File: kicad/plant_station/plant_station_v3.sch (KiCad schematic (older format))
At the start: 12 parts, among them J10 I2C HOST, J13 MB_I2C, J2 MB_I2C, J4 MB_I2C, J5 MB_I2C, J6 MB_I2C, J9 I2C SCREEN

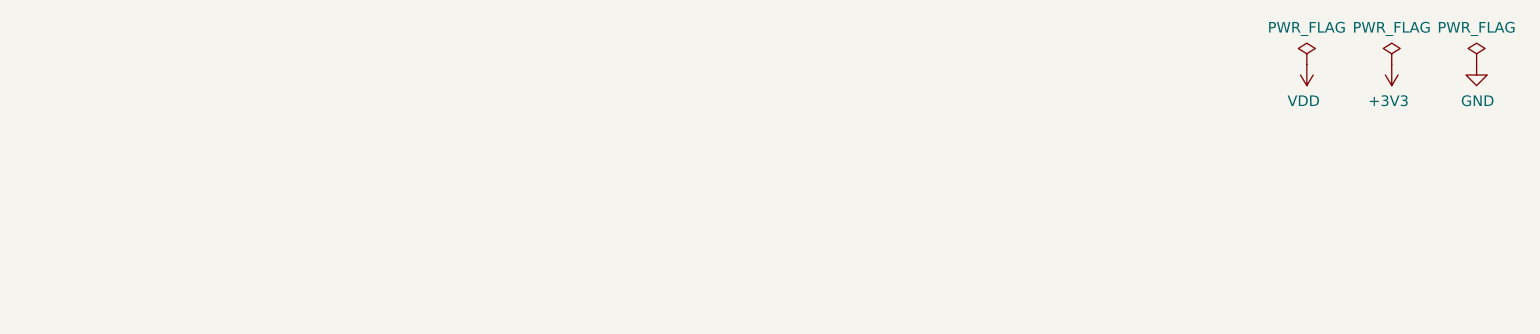
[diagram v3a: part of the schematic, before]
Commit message: Pre-refactoring, diagnostics complete, timer not working properly
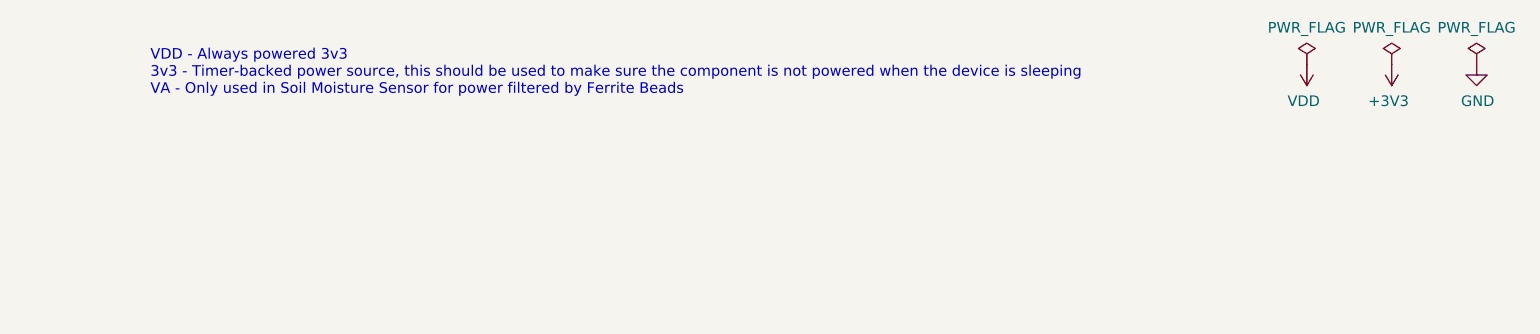
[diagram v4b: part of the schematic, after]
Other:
- note added: "VDD - Always powered 3v3\n3v3 - Timer-backed power source, this should be used to make sure the component is not powered when the device is sleeping\nVA - Only used in Soil Moisture Sensor for power filtered by Ferrite Beads"
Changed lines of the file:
@@
 NoConn ~ 2400 2450
 NoConn ~ 2400 2350
+Text Notes 4700 950  0    50   ~ 0
+VDD - Always powered 3v3\n3v3 - Timer-backed power source, this should be used to make sure the component is not powered when the device is sleeping\nVA - Only used in Soil Moisture Sensor for power filtered by Ferrite Beads
 $EndSCHEMATC
